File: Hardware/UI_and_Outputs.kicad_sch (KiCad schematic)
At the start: 8 parts

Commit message: Major Updates to Schematic
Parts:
- added J4: RGB-TFT Screen, Custom_Screens:1.8_128x160_RGB-TFT, symbol Connector:Conn_01x08_Socket
- added SW1: RotaryEncoder_Switch, symbol Device:RotaryEncoder_Switch
- R1, R2, R3, R4: value R -> 510
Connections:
- net GND: now also J4.1 (Pin_1)
- net GPIO 2: now reaches R2.1
- net GPIO 13: now reaches R3.1
- net GPIO 15: now reaches R1.1
- net GPIO 14: now reaches R4.1
- new net +3V3: J4.2 (Pin_2), J4.8 (Pin_8)
- new net Enc_A: SW1.A
- new net Enc_B: SW1.C
- new net Enc_SW: SW1.B
- new net MOSI: J4.4 (Pin_4)
- new net SCK: J4.3 (Pin_3)
- new net TFT_CS: J4.7 (Pin_7)
- new net TFT_DC: J4.6 (Pin_6)
- new net TFT_RST: J4.5 (Pin_5)
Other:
- note added: "LED's"
- note added: "Screen/Display"

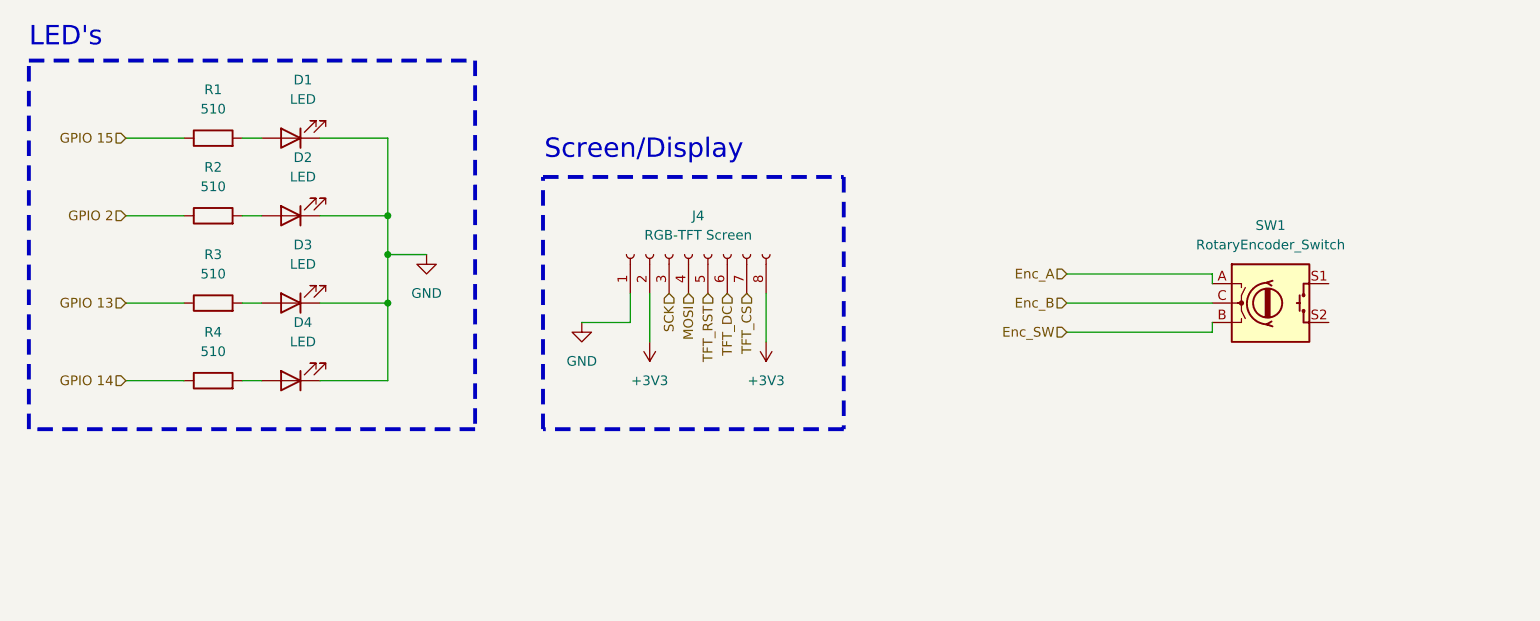
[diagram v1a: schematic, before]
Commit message: Schematic V0.9 is complete
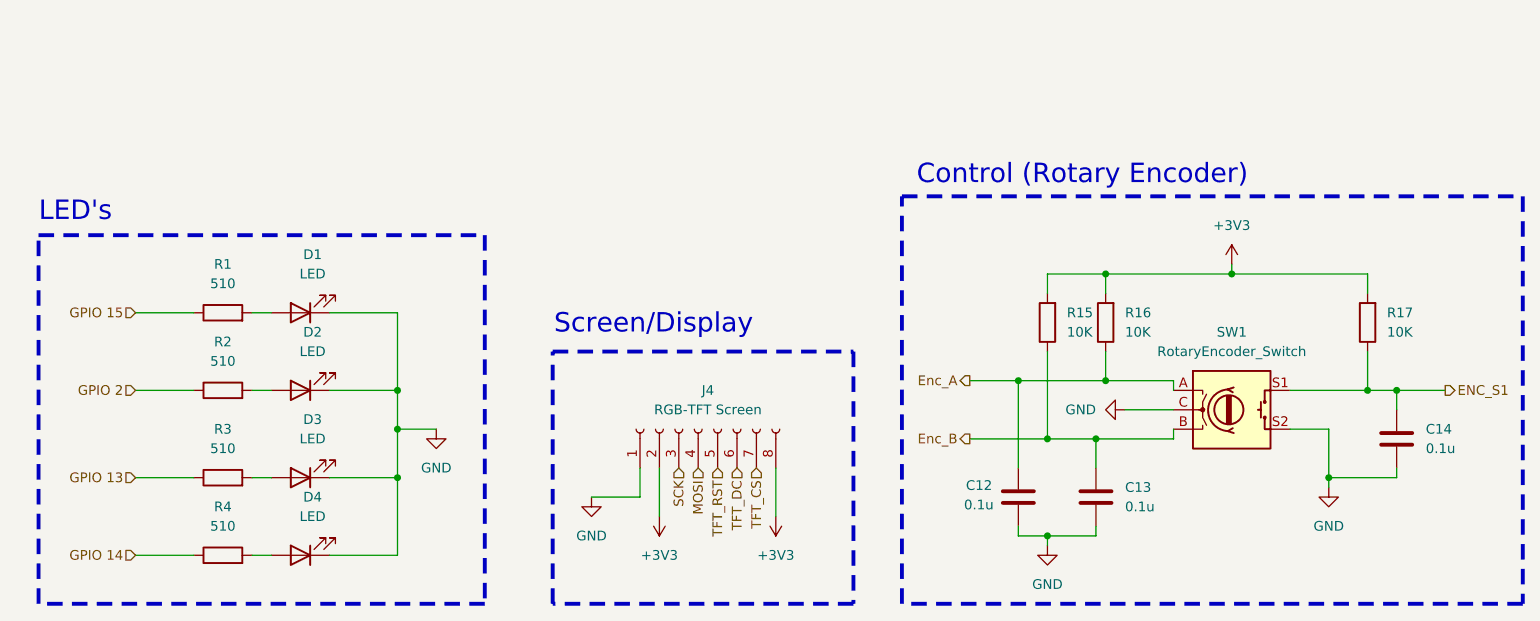
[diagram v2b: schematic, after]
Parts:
- added C12, C13, C14: 0.1u, Capacitor_SMD:C_0805_2012Metric, symbol Device:C
- added R15, R16, R17: 10K, Resistor_SMD:R_0805_2012Metric, symbol Device:R
- D1, D2, D3, D4: footprint (none) -> LED_THT:LED_D3.0mm
- R1, R2, R3, R4: footprint (none) -> Resistor_SMD:R_0805_2012Metric
- SW1: footprint (none) -> Rotary_Encoder:RotaryEncoder_Alps_EC11E-Switch_Vertical_H20mm; LCSC (none) -> C202365
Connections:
- net Enc_SW is gone; now on net Enc_B: SW1.B
- net +3V3: now also R15.2, R16.2, R17.2
- net Enc_A: now also C12.1, R16.1
- net Enc_B: now also C13.1, R15.1; no longer SW1.C
- net GND: now also SW1.C, SW1.S2, C12.2, C13.2, C14.2
- net ENC_S1: now reaches SW1.S1
- net ENC_S1: now also C14.1, R17.1
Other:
- note added: "Control (Rotary Encoder)"
- moved on the sheet: D1, D2, D3, D4, J4, R1, R2, R3, R4, SW1
